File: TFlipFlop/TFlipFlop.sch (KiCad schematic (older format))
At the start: 5 parts, among them U1 74LS08, U2 74LS08, U3 74LS02, U4 74LS04

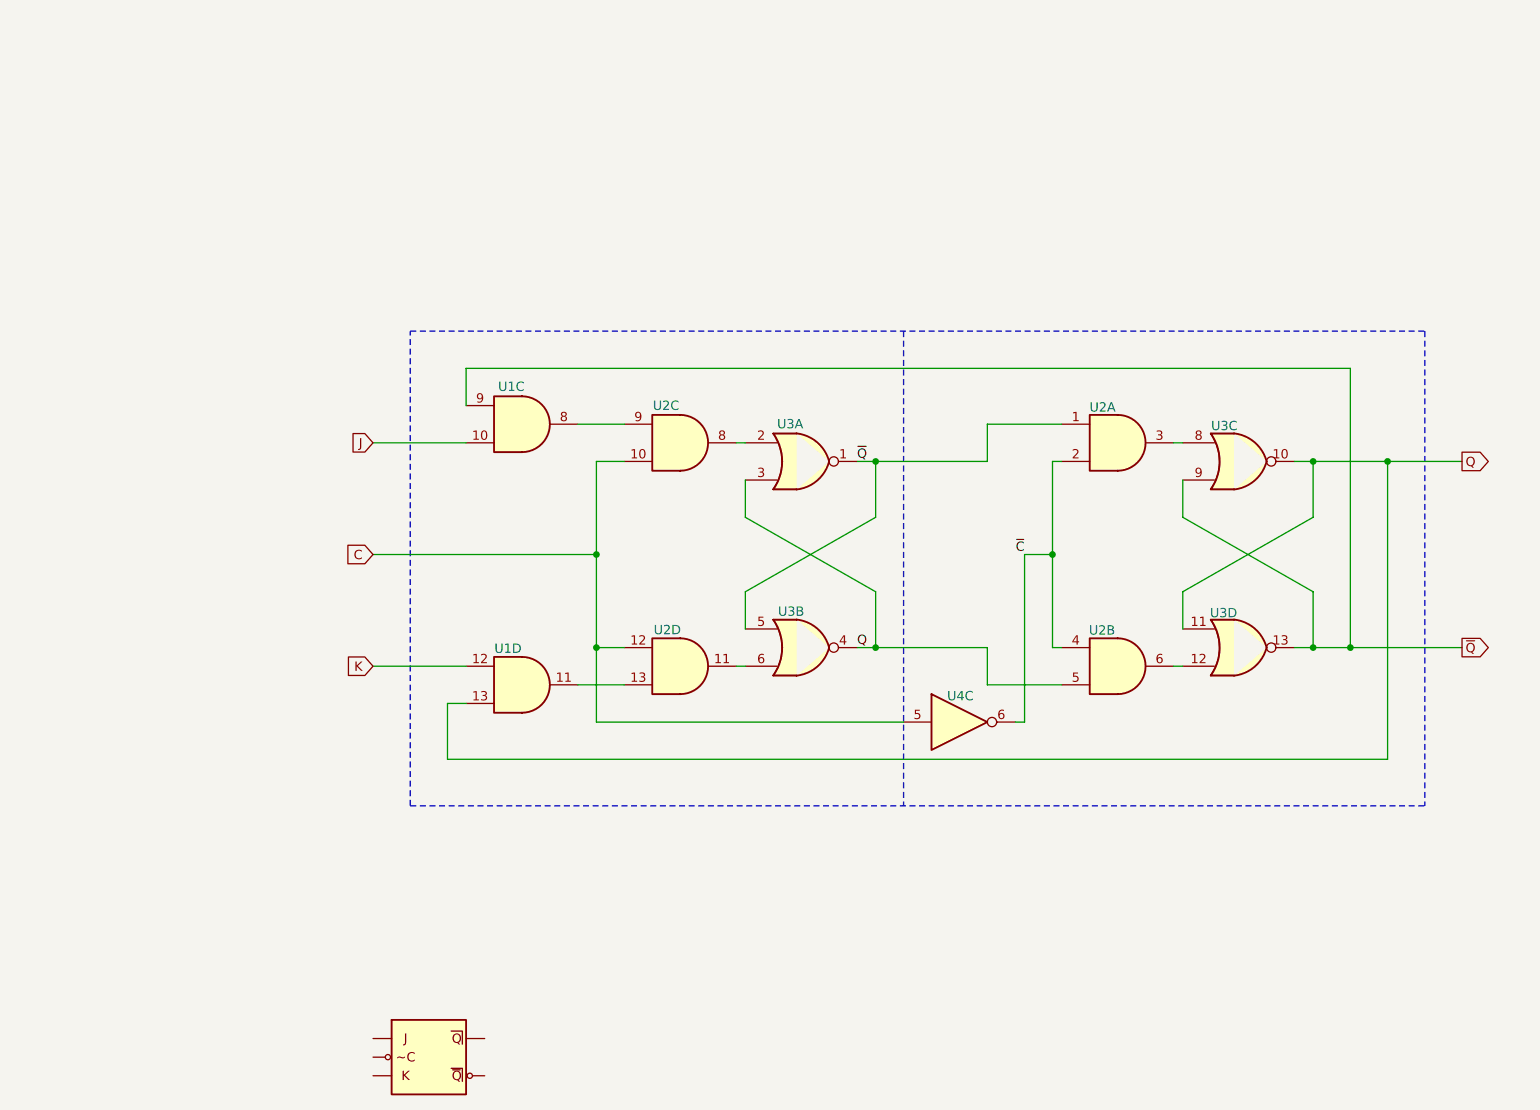
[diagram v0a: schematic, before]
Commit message: add D and T Latch
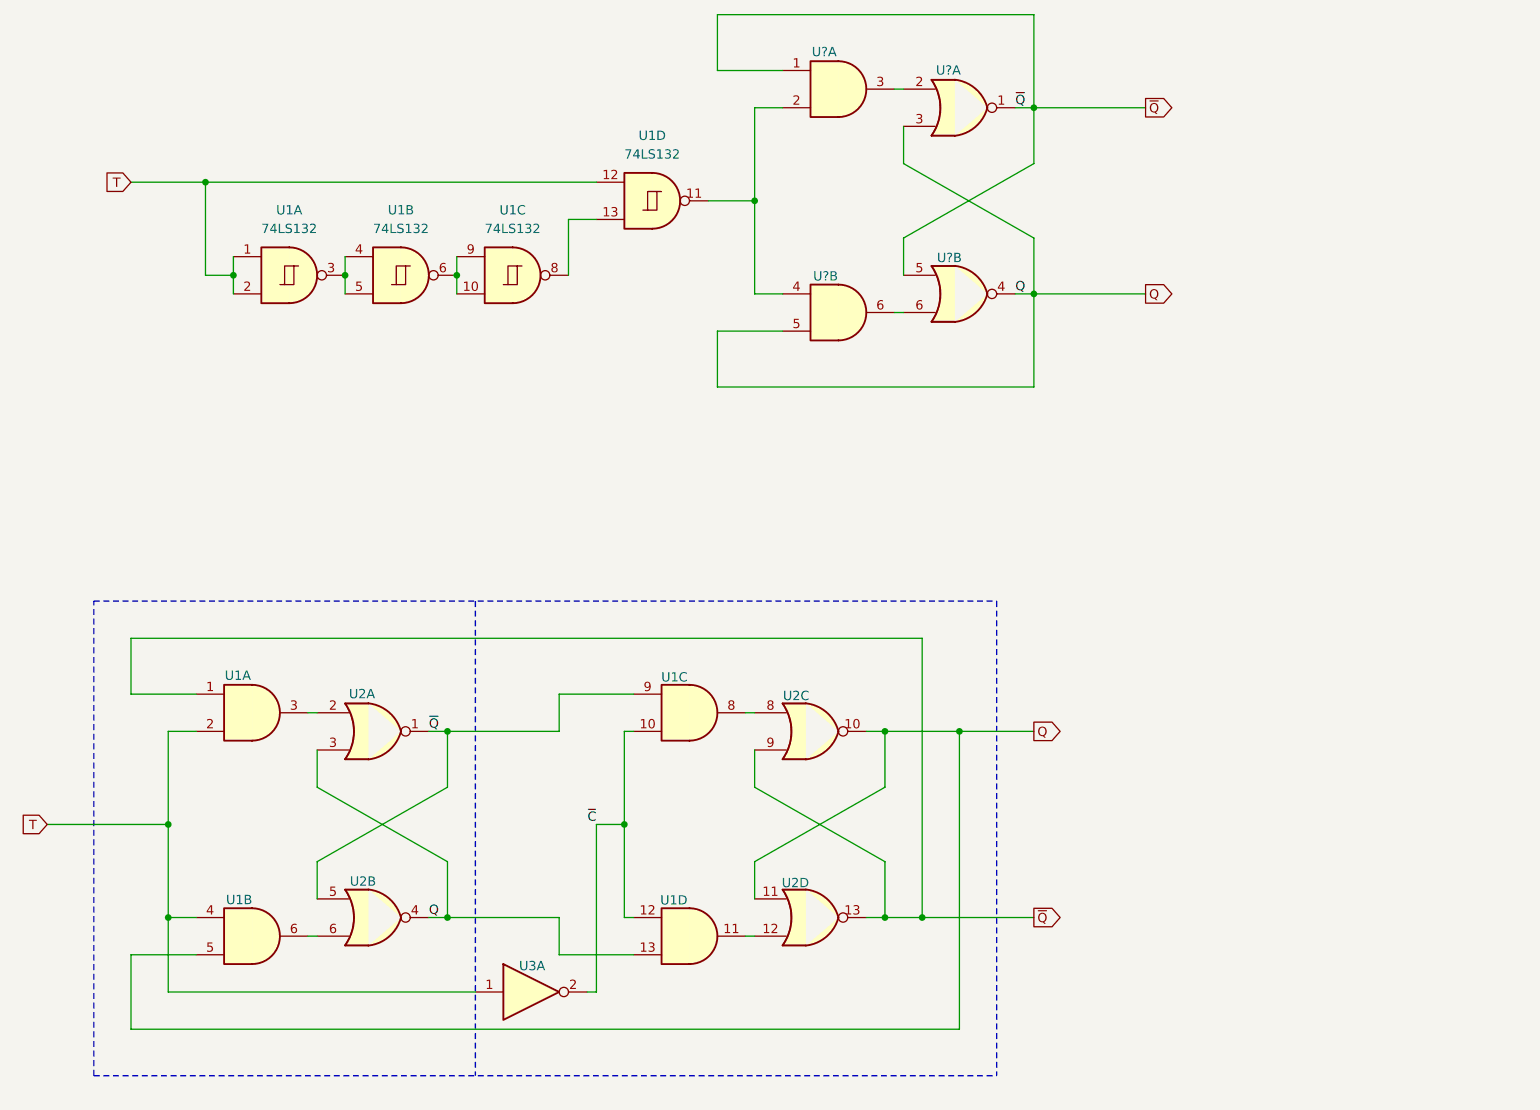
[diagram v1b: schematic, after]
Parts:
- removed U1: 74LS08, symbol 74xx:74LS08
- removed U?: JK_MS, symbol 00TJR:JK_MS
- added U1: 74LS132, symbol 74xx:74LS132
- added U? (x2): 74LS02, symbol 74xx:74LS02
- added U? (x2): 74LS08, symbol 74xx:74LS08
- renumbered U2 to U1, U3 to U2, U4 to U3
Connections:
- net Q: now also U1.13, U1.5, U?.3, U?.4, U?.5; no longer U1.5
- net ~C: now also U1.10, U1.12, U3.2; no longer U1.2, U1.4, U3.6
- net ~Q: now also U1.1, U1.9, U?.1, U?.1, U?.5; no longer U1.1
- net at U2.2: now also U1.3; no longer U1.8
- net at U2.6: now also U1.6; no longer U1.11
- net at U2.12: now also U1.11; no longer U1.6
- net at U2.8: now also U1.8; no longer U1.3
- removed net C: U1.10, U1.12, U3.5
- new net: U1.3, U1.4, U1.5
- new net: U1.10, U1.6, U1.9
- new net: U1.13, U1.8
- new net: U1.11, U?.2, U?.4
- new net: U?.6, U?.6
- new net: U?.2, U?.3
- new net T: U1.1, U1.12, U1.2, U1.2, U1.4, U3.1
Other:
- moved on the sheet: U2A, U2B, U2C, U2D
